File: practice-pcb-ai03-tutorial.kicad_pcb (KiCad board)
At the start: 2 copper layers, 100.8 x 57.2 mm, 34 parts, among them SW1 MX-NoLED, SW2 MX-NoLED, SW3 MX-NoLED, SW4 MX-NoLED, SW5 MX-NoLED, SW6 MX-NoLED, SW7 MX-NoLED, SW8 MX-NoLED, SW9 MX-NoLED, U1 ATmega32U4-AU, Y1 16MHz

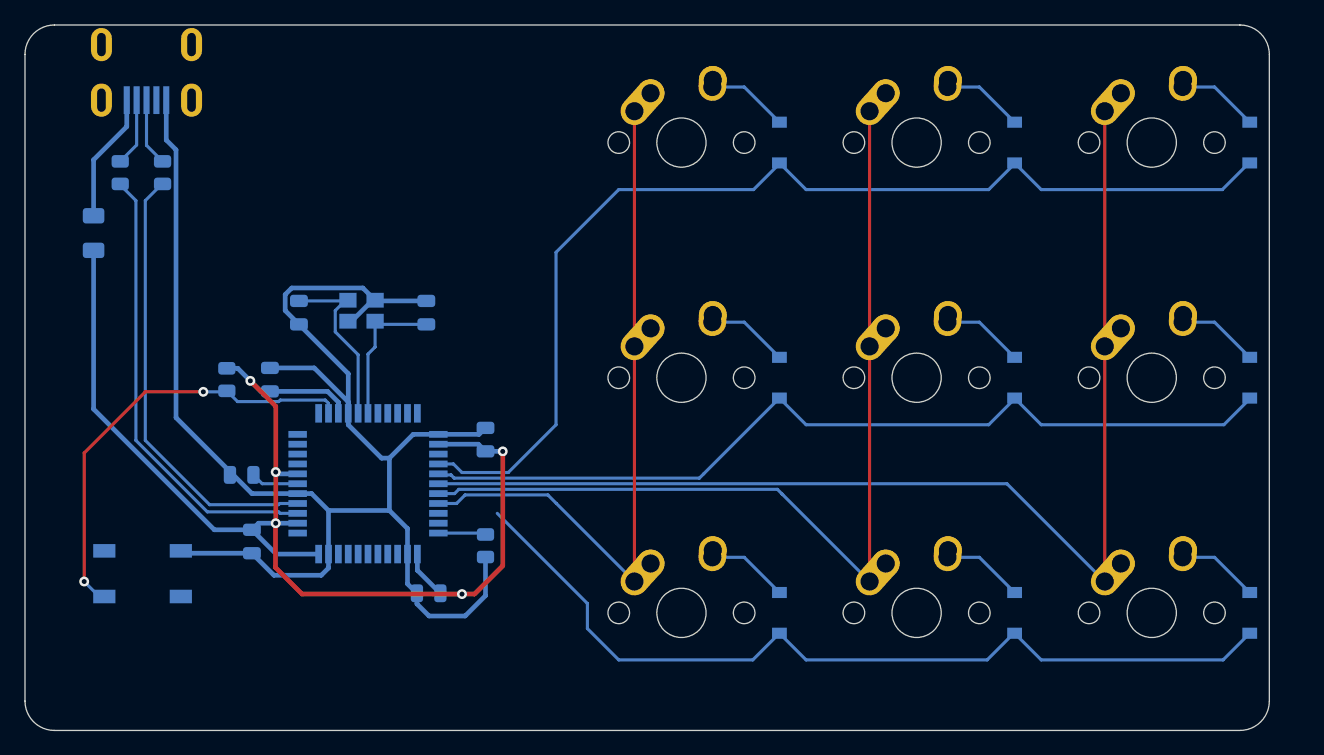
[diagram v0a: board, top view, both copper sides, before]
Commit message: chore(pcb): add hotswap socket for switches
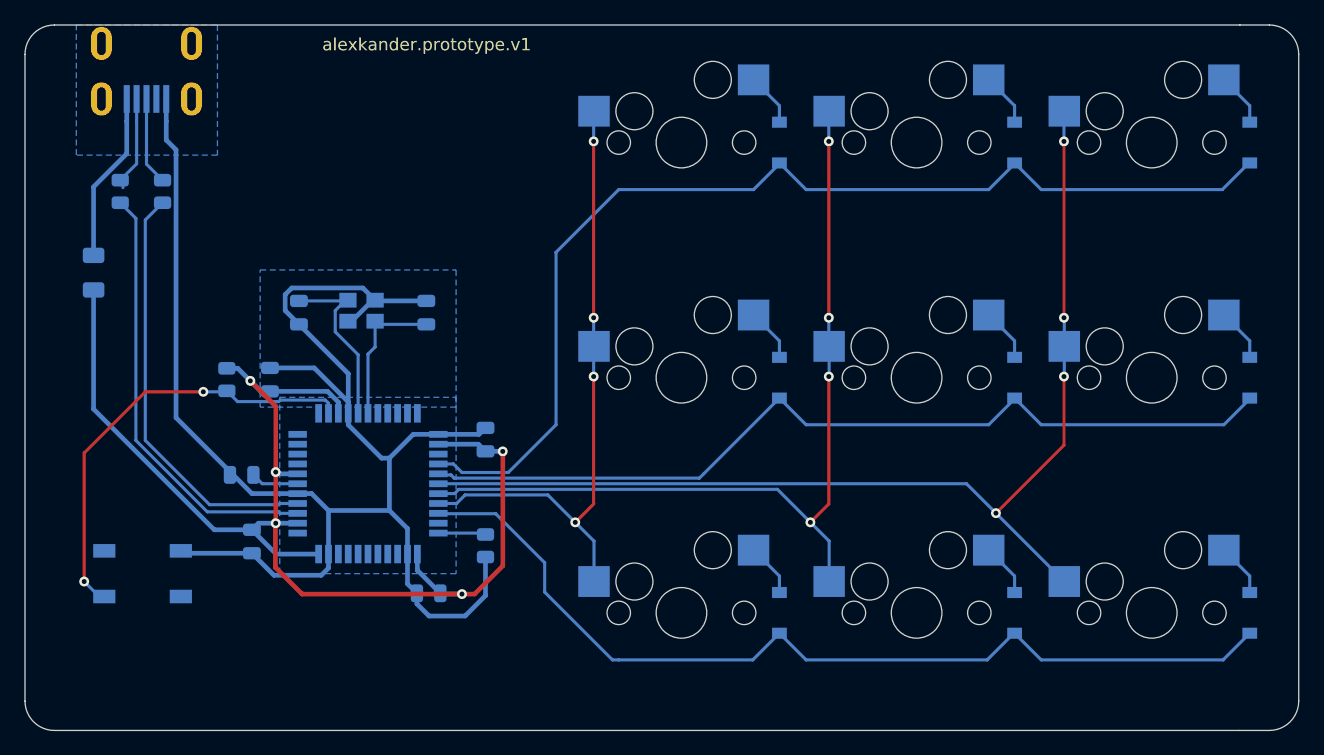
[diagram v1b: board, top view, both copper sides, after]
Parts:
- SW1, SW2, SW3, SW4, SW5, SW6, SW7, SW8, SW9: footprint MX_Alps_Hybrid:MX-1U-NoLED -> kbd:CherryMX_Hotswap
- moved F1 3.21 mm to (-47.6, 10.5)
- moved R1 1.52 mm to (-45.5, 3.96)
- moved R2 1.52 mm to (-42.0, 3.96)
- moved USB1 0.10 mm to (-43.3, -8.03)
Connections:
- U1 pad 1: Net-(U1-Pad1) -> (no net)
- U1 pad 10: Net-(U1-Pad10) -> (no net)
- U1 pad 11: Net-(U1-Pad11) -> (no net)
- U1 pad 12: Net-(U1-Pad12) -> (no net)
- U1 pad 18: Net-(U1-Pad18) -> (no net)
- U1 pad 19: Net-(U1-Pad19) -> (no net)
- U1 pad 20: Net-(U1-Pad20) -> (no net)
- U1 pad 21: Net-(U1-Pad21) -> (no net)
- U1 pad 22: Net-(U1-Pad22) -> (no net)
- U1 pad 25: Net-(U1-Pad25) -> (no net)
- U1 pad 32: Net-(U1-Pad32) -> (no net)
- U1 pad 36: Net-(U1-Pad36) -> (no net)
- U1 pad 37: Net-(U1-Pad37) -> (no net)
- U1 pad 38: Net-(U1-Pad38) -> (no net)
- U1 pad 39: Net-(U1-Pad39) -> (no net)
- U1 pad 40: Net-(U1-Pad40) -> (no net)
- U1 pad 41: Net-(U1-Pad41) -> (no net)
- U1 pad 42: Net-(U1-Pad42) -> (no net)
- U1 pad 8: Net-(U1-Pad8) -> (no net)
- U1 pad 9: Net-(U1-Pad9) -> (no net)
- USB1 pad 2: Net-(USB1-Pad2) -> (no net)
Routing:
- net COL2: track 95.4 -> 88.9 mm, vias 0 -> 4
- net COL1: track 76.4 -> 70.8 mm, vias 0 -> 4
- net COL0: track 57.2 -> 51.9 mm, vias 0 -> 4
- net ROW2: track 71.9 -> 77.0 mm
- net VCC: track 10.5 -> 13.8 mm
- net +5V: track 110.0 -> 106.8 mm
- net Net-(D4-Pad2): track 6.62 -> 4.30 mm
- net Net-(D7-Pad2): track 6.62 -> 4.30 mm
- net Net-(D6-Pad2): track 6.62 -> 4.30 mm
- net Net-(D5-Pad2): track 6.62 -> 4.30 mm
- net Net-(D1-Pad2): track 6.62 -> 4.30 mm
- net Net-(D9-Pad2): track 6.62 -> 4.30 mm
- net Net-(D8-Pad2): track 6.62 -> 4.30 mm
- net Net-(D2-Pad2): track 6.62 -> 4.30 mm
- net Net-(D3-Pad2): track 6.62 -> 4.36 mm
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- added copper zone on B.Cu, net GND
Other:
- board size 100.8 x 57.2 mm -> 103.2 x 57.2 mm
- rule pad_to_mask_clearance: 0 -> 0.2
- board text added: "alexkander.prototype.v1"

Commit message: cambios
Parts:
- moved R3 1.86 mm to (-36.8, 21.1)
- moved C1 1.30 mm to (-21.8, 36.5)
- moved C6 0.94 mm to (-34.8, 27.4), turned to 270 degrees
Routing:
- net +5V: track 106.8 -> 127.2 mm, vias 5 -> 4
- net GND: track 136.1 -> 145.7 mm
- net Net-(R3-Pad2): track 35.8 -> 32.0 mm
